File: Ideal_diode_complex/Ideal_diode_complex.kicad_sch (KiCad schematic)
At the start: 15 parts, among them CN1 24_243_1, CN2 24_243_1, CN3 24_243_2, CN4 24_243_2, Q1 SI7336ADP-T1-GE3-HXY, U1 LTC4352IMS_PBF

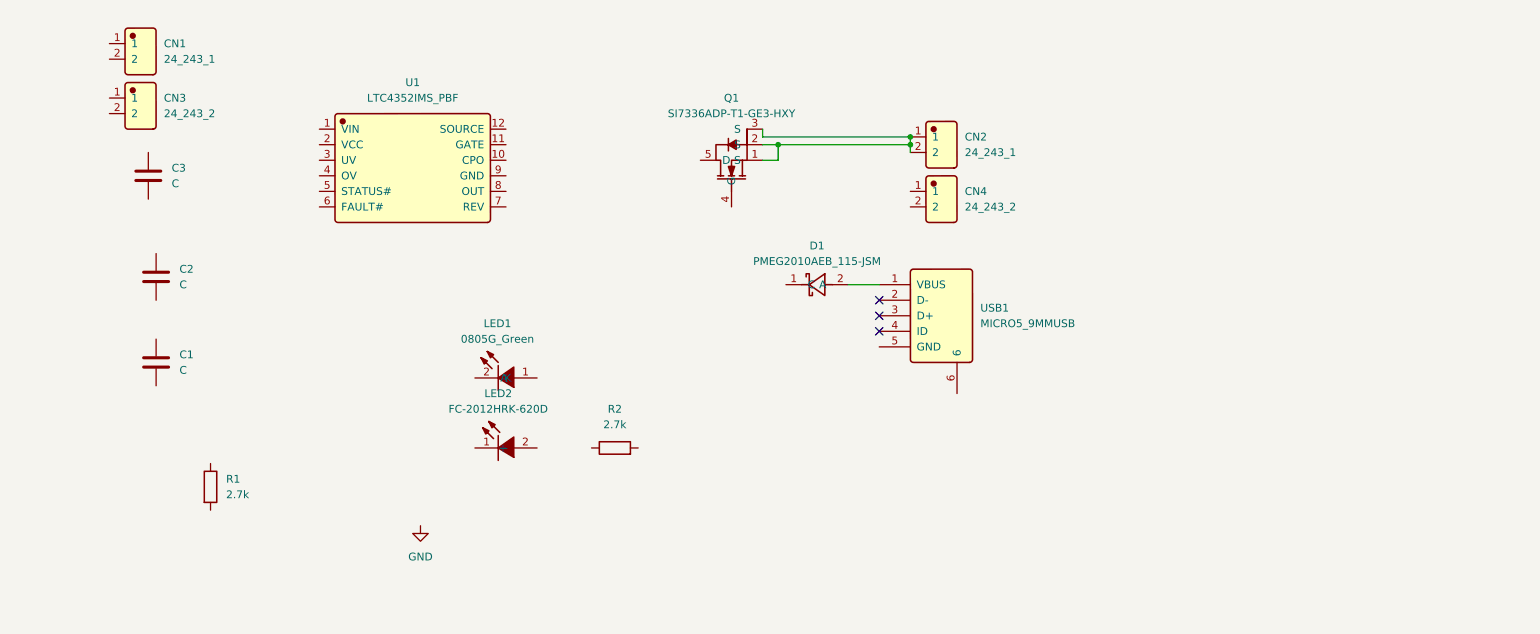
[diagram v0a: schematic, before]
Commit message: Finished complex ideal diode PCB
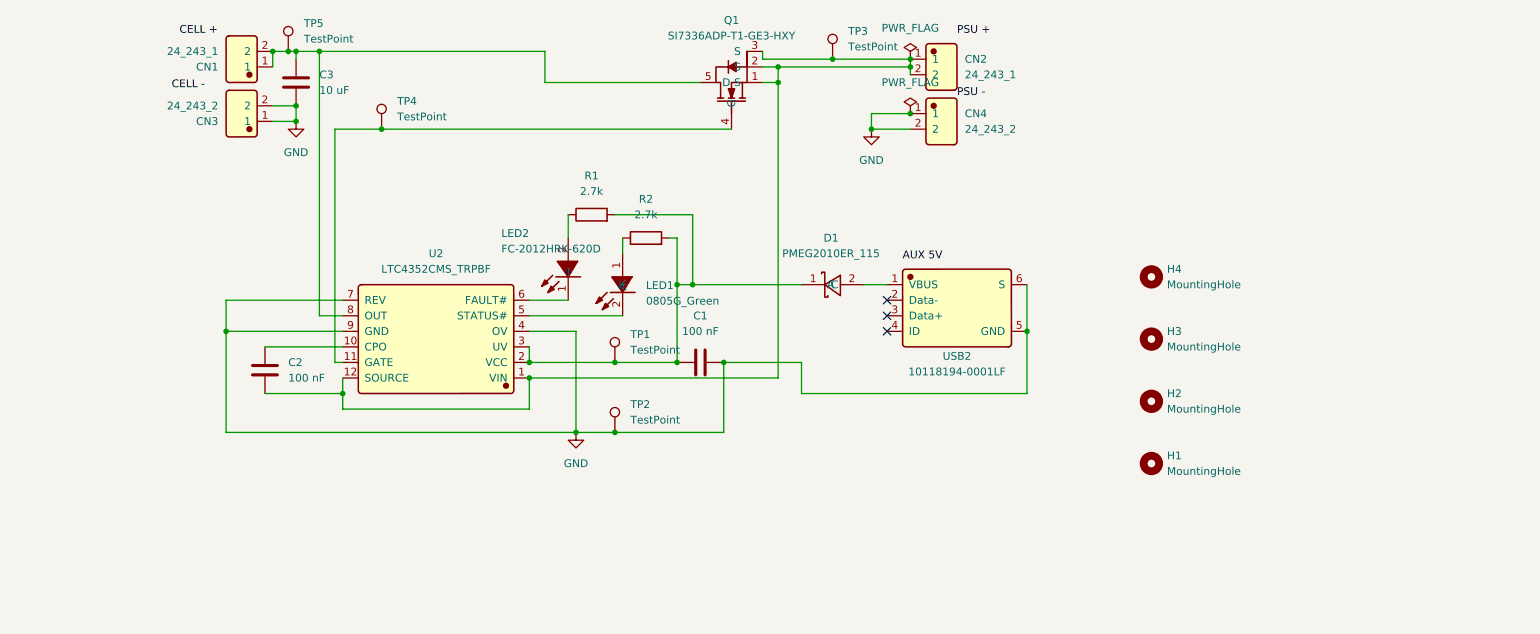
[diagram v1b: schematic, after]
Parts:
- removed D1: PMEG2010AEB_115-JSM, JLCImport:PMEG2010AEB_115-JSM, symbol JLCImport:PMEG2010AEB_115-JSM
- removed U1: LTC4352IMS_PBF, JLCImport:LTC4352IMS_PBF, symbol JLCImport:LTC4352IMS_PBF
- removed USB1: MICRO5_9MMUSB, JLCImport:MICRO5_9MMUSB, symbol JLCImport:MICRO5_9MMUSB
- added D1: PMEG2010ER_115, JLCImport:PMEG2010ER_115, symbol JLCImport:PMEG2010ER_115
- added H1, H2, H3, H4: MountingHole, MountingHole:MountingHole_2.7mm_M2.5, symbol Mechanical:MountingHole
- added TP1, TP2, TP3, TP4, TP5: TestPoint, TestPoint:TestPoint_Pad_D1.0mm, symbol Connector:TestPoint
- added U2: LTC4352CMS_TRPBF, JLCImport:LTC4352CMS_TRPBF, symbol JLCImport:LTC4352CMS_TRPBF
- added USB2: 10118194-0001LF, JLCImport:10118194-0001LF, symbol JLCImport:10118194-0001LF
- C1, C2: value C -> 100 nF; footprint (none) -> Capacitor_SMD:C_0603_1608Metric
- C3: value C -> 10 uF; footprint (none) -> Capacitor_SMD:C_1206_3216Metric
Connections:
- net GND: now also C1.2, C3.2, CN3.1, CN3.2, CN4.1, CN4.2, TP2.1, U2.4 (OV), U2.7 (REV), U2.9 (GND), USB2.5 (GND), USB2.6 (S)
- net at CN2.1, CN2.2, Q1.1 (S)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: now also C2.2, TP3.1, U2.1 (VIN), U2.12 (SOURCE)
- net at C2.1: now also U2.10 (CPO)
- net at C1.1: now also R1.2, R2.2, D1.1 (C), TP1.1, U2.2 (VCC), U2.3 (UV)
- net at R1.1: now also LED2.2 (+)
- net at CN1.1: now also C3.1, CN1.2, Q1.5 (D), TP5.1, U2.8 (OUT)
- net at Q1.4 (G): now also TP4.1, U2.11 (GATE)
- net at LED1.1 (A): now also R2.1
- net at LED1.2 (K): now also U2.5 (STATUS#)
- net at LED2.1 (-): now also U2.6 (FAULT#)
- new net: D1.2 (A), USB2.1 (VBUS)
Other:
- moved on the sheet: C1, C2, C3, CN1, CN2, CN3, CN4, LED1, LED2, Q1, R1, R2

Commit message: Added a boost converter to the USB line to make sure VCC stays above 4.7V
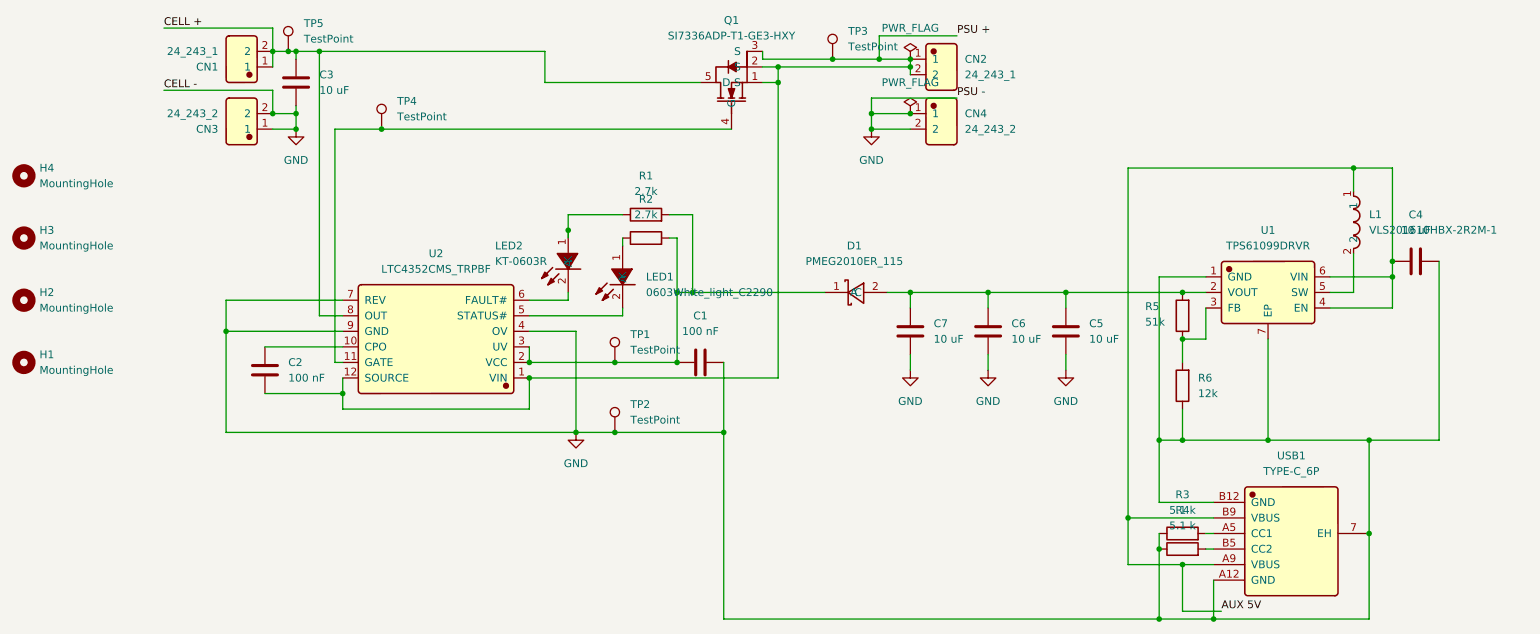
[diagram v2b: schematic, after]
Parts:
- removed LED1: 0805G_Green, JLCImport:0805G_Green, symbol JLCImport:0805G_Green
- removed LED2: FC-2012HRK-620D, JLCImport:FC-2012HRK-620D, symbol JLCImport:FC-2012HRK-620D
- removed USB2: 10118194-0001LF, JLCImport:10118194-0001LF, symbol JLCImport:10118194-0001LF
- added C4, C5, C6, C7: 10 uF, Capacitor_SMD:C_0402_1005Metric, symbol Device:C
- added L1: VLS201610HBX-2R2M-1, JLCImport:VLS201610HBX-2R2M-1, symbol JLCImport:VLS201610HBX-2R2M-1
- added LED1: 0603White_light_C2290, JLCImport:0603White_light_C2290, symbol JLCImport:0603White_light_C2290
- added LED2: KT-0603R, JLCImport:KT-0603R, symbol JLCImport:KT-0603R
- added R3, R4: 5.1 k, Resistor_SMD:R_0402_1005Metric, symbol Device:R
- added R5: 51k, Resistor_SMD:R_0402_1005Metric, symbol Device:R
- added R6: 12k, Resistor_SMD:R_0402_1005Metric, symbol Device:R
- added U1: TPS61099DRVR, JLCImport:TPS61099DRVR, symbol JLCImport:TPS61099DRVR
- added USB1: TYPE-C_6P, JLCImport:TYPE-C_6P, symbol JLCImport:TYPE-C_6P
- C1, C2: footprint Capacitor_SMD:C_0603_1608Metric -> Capacitor_SMD:C_0402_1005Metric
- R1, R2: footprint Resistor_SMD:R_0805_2012Metric -> Resistor_SMD:R_0603_1608Metric
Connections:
- net AUX 5V: now also C4.1, L1.1, U1.4 (EN), U1.6 (VIN), USB1.A9 (VBUS), USB1.B9 (VBUS)
- net CELL +: now also C3.1, CN1.1, CN1.2, Q1.5 (D), TP5.1, U2.8 (OUT)
- net GND: now also C4.2, C5.2, C6.2, C7.2, R3.1, R4.1, R6.1, U1.1 (GND), U1.7 (EP), USB1.7 (EH), USB1.A12 (GND), USB1.B12 (GND)
- net PSU +: now also C2.2, CN2.1, CN2.2, Q1.1 (S), Q1.2 (S), Q1.3 (S), TP3.1, U2.1 (VIN), U2.12 (SOURCE)
- net at U2.5 (STATUS#): now also LED1.2 (K)
- net at U2.6 (FAULT#): now also LED2.2 (K)
- net at D1.2 (A): now also C5.1, C6.1, C7.1, R5.2, U1.2 (VOUT)
- net at R1.1: now also LED2.1 (A)
- net at R2.1: now also LED1.1 (A)
- new net: R4.2, USB1.B5 (CC2)
- new net: R5.1, R6.2, U1.3 (FB)
- new net: L1.2, U1.5 (SW)
- new net: R3.2, USB1.A5 (CC1)
- no-connect marks 3 -> 0
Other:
- moved on the sheet: CN3, D1, H1, H2, H3, H4, R1

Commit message: updated to use different voltage regulator smd to be cheaper
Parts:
- removed C7: 10 uF, Capacitor_SMD:C_0402_1005Metric, symbol Device:C
- removed D1: PMEG2010ER_115, JLCImport:PMEG2010ER_115, symbol JLCImport:PMEG2010ER_115
- removed L1: VLS201610HBX-2R2M-1, JLCImport:VLS201610HBX-2R2M-1, symbol JLCImport:VLS201610HBX-2R2M-1
- removed U1: TPS61099DRVR, JLCImport:TPS61099DRVR, symbol JLCImport:TPS61099DRVR
- added D1, D2: B5819W_C8598, JLCImport:B5819W_C8598, symbol JLCImport:B5819W_C8598
- added L1: MWSA0402S-100MT, JLCImport:MWSA0402S-100MT, symbol JLCImport:MWSA0402S-100MT
- added U1: TPS61041DBVR, JLCImport:TPS61041DBVR, symbol JLCImport:TPS61041DBVR
- C4: value 10 uF -> 22 uF; footprint Capacitor_SMD:C_0402_1005Metric -> Capacitor_SMD:C_1206_3216Metric
- C5: value 10 uF -> 47 uF; footprint Capacitor_SMD:C_0402_1005Metric -> Capacitor_SMD:C_1206_3216Metric
- C6: value 10 uF -> 10 nF
- R1, R2: value 2.7k -> 2.7 k
- R5: value 51k -> 18 k; footprint Resistor_SMD:R_0402_1005Metric -> Resistor_SMD:R_0603_1608Metric
- R6: value 12k -> 5.1 k; footprint Resistor_SMD:R_0402_1005Metric -> Resistor_SMD:R_0603_1608Metric
- TP1, TP2, TP3, TP4, TP5: now left out of the parts list
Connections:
- net AUX 5V: no longer C4.1, USB1.A9 (VBUS), USB1.B9 (VBUS)
- net GND: now also C5.1, R6.2, U1.2 (GND); no longer C5.2, C6.2, R6.1
- net at C1.1, R1.2, R2.2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: now also D2.1 (-)
- net at R5.1: now also C5.2, C6.1, D1.1 (-), D2.2 (+); no longer R6.2
- new net: C6.2, R5.2, R6.1, U1.3 (FB)
- new net: C4.1, L1.1, U1.4 (EN), U1.5 (VIN), USB1.A9 (VBUS), USB1.B9 (VBUS)
- new net: D1.2 (+), L1.2, U1.1 (SW)
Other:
- moved on the sheet: R3, R4, USB1

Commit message: Final design
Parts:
- removed C5: 47 uF, Capacitor_SMD:C_1206_3216Metric, symbol Device:C
- removed C6: 10 nF, Capacitor_SMD:C_0402_1005Metric, symbol Device:C
- removed D1, D2: B5819W_C8598, JLCImport:B5819W_C8598, symbol JLCImport:B5819W_C8598
- removed L1: MWSA0402S-100MT, JLCImport:MWSA0402S-100MT, symbol JLCImport:MWSA0402S-100MT
- removed R5: 18 k, Resistor_SMD:R_0603_1608Metric, symbol Device:R
- removed R6: 5.1 k, Resistor_SMD:R_0603_1608Metric, symbol Device:R
- removed U1: TPS61041DBVR, JLCImport:TPS61041DBVR, symbol JLCImport:TPS61041DBVR
- added TP6: TestPoint, TestPoint:TestPoint_Pad_D1.0mm, symbol Connector:TestPoint
- added U1: MAX40200AUK_T, JLCImport:MAX40200AUK_T, symbol JLCImport:MAX40200AUK_T
- C3: value 10 uF -> 1 uF; footprint Capacitor_SMD:C_1206_3216Metric -> Capacitor_SMD:C_0402_1005Metric
- C4: value 22 uF -> 1 uF; footprint Capacitor_SMD:C_1206_3216Metric -> Capacitor_SMD:C_0402_1005Metric
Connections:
- net CELL +: no longer C3.1
- net GND: now also C3.1, C4.1, U1.2 (GND); no longer C3.2, C4.2
- net at C1.1, R1.2, R2.2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: now also C3.2, U1.5 (OUT)
- net at USB1.A9 (VBUS), USB1.B9 (VBUS): now also C4.2, TP6.1, U1.1 (VDD), U1.3 (EN); no longer C4.1
- no-connect marks 0 -> 1
